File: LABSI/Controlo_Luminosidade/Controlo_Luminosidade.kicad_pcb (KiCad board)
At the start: 2 copper layers, 86 x 71 mm, 38 parts, among them J1 Barrel_Jack_Switch, J2 Barrel_Jack_Switch, J3 Conn_01x05_Pin, J5 Conn_01x04_Pin, J6 AVR-ISP-6, J7 Conn_01x03_Pin, J8 Conn_01x03_Pin, J9 Conn_01x05_Pin, Q1 IRLZ24, U1 ATmega328-P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

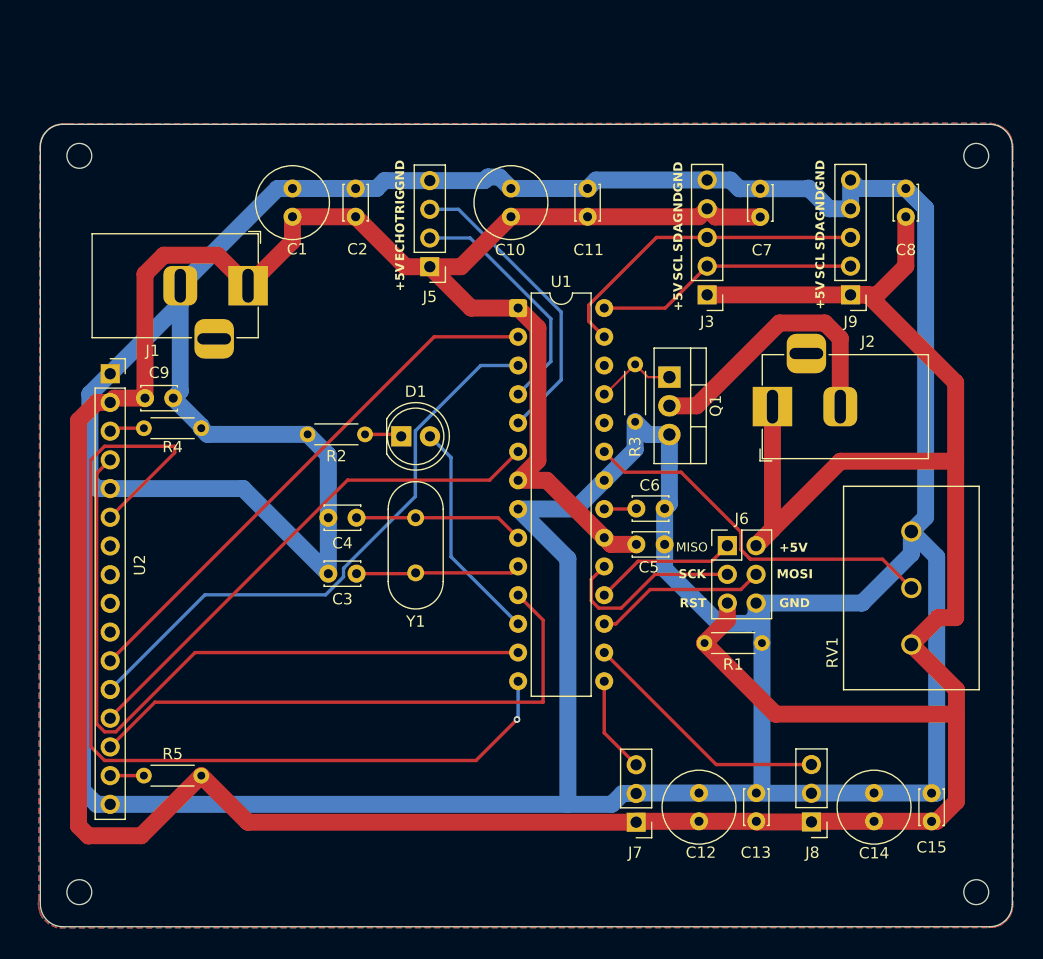
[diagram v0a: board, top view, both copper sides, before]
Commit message: added lcd through i2c, code for timer1(servo)
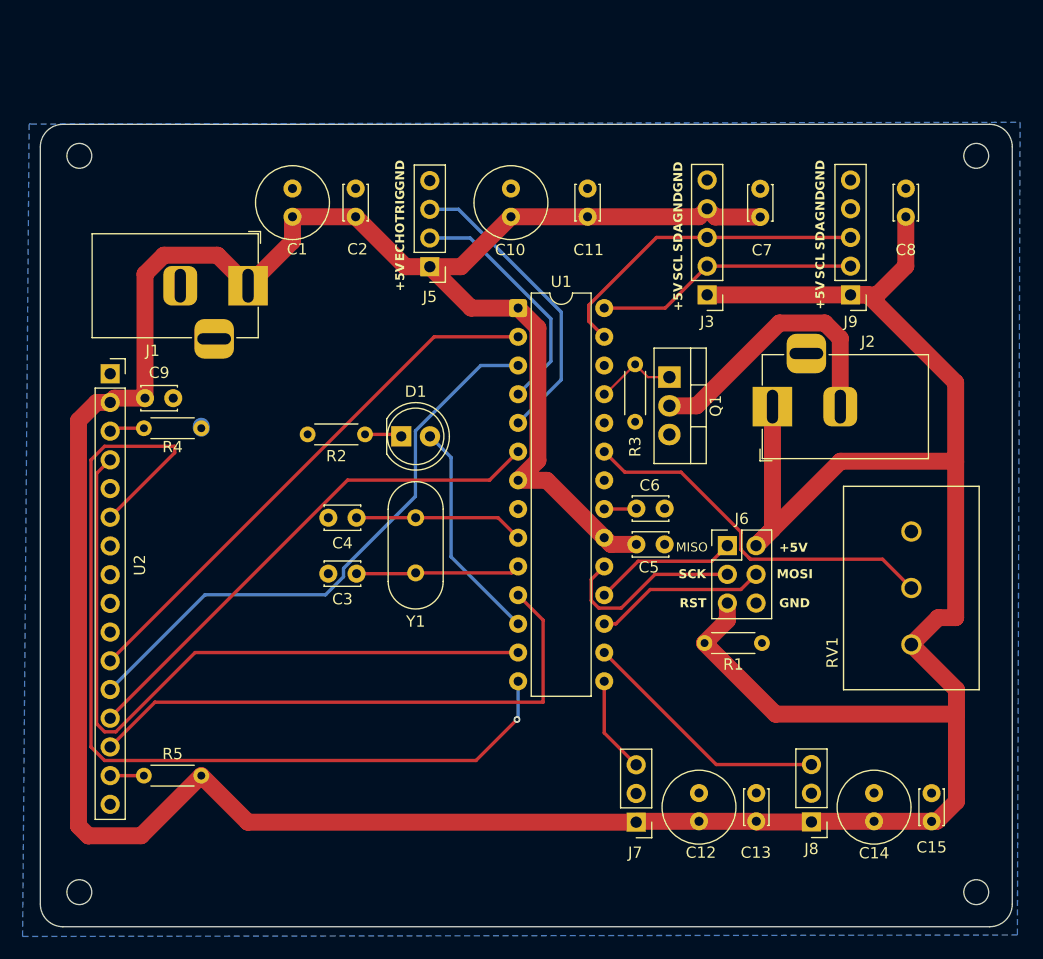
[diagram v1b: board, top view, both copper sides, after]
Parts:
- R2: value 220 -> 330
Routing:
- net GND: track 418.3 -> 0.30 mm
- removed copper zone on F.Cu, net GND

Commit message: botoes touch sem debounce a funcionar, logica motor a funcionar
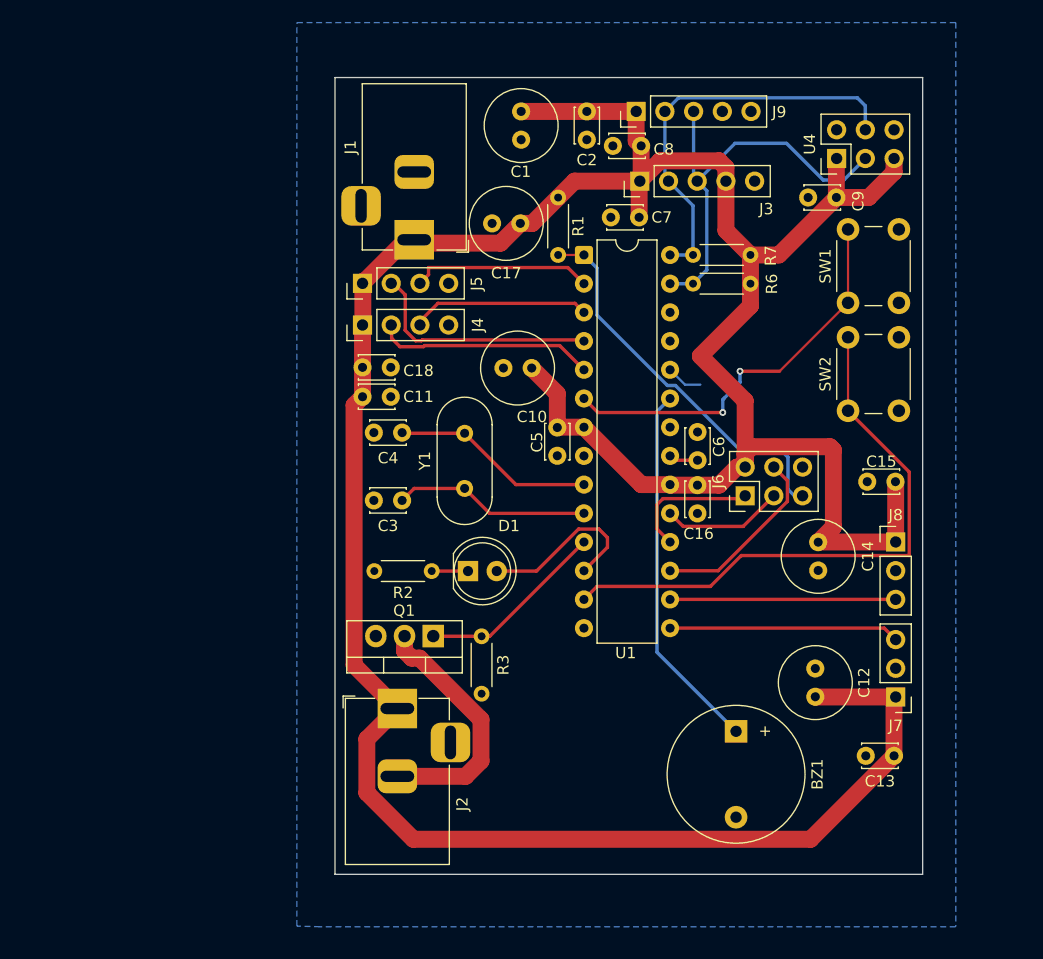
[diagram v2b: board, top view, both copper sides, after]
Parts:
- removed R4: 1k, Resistor_THT:R_Axial_DIN0204_L3.6mm_D1.6mm_P5.08mm_Horizontal
- removed R5: 220, Resistor_THT:R_Axial_DIN0204_L3.6mm_D1.6mm_P5.08mm_Horizontal
- removed REF** (x4): MountingHole_2.2mm_M2, MountingHole:MountingHole_2.2mm_M2
- removed RV1: R_Potentiometer, P160KN-0QC15B500K:P160
- removed U2: LCD1602A, Connector_PinSocket_2.54mm:PinSocket_1x16_P2.54mm_Vertical
- added BZ1: Buzzer, Buzzer_Beeper:Buzzer_12x9.5RM7.6, F.Cu at (160.6, 107.7)
- added C16: 0.1u, Capacitor_THT:C_Disc_D3.0mm_W2.0mm_P2.50mm, F.Cu at (157.1, 85.9)
- added C17: 10u, Capacitor_THT:C_Radial_D6.3mm_H11.0mm_P2.50mm, F.Cu at (141.5, 62.8)
- added C18: 0.1u, Capacitor_THT:C_Disc_D3.0mm_W2.0mm_P2.50mm, F.Cu at (127.5, 75.5)
- added J4: Conn_01x04_Pin, Connector_PinHeader_2.54mm:PinHeader_1x04_P2.54mm_Vertical, F.Cu at (127.5, 71.8)
- added R6: 10k, Resistor_THT:R_Axial_DIN0204_L3.6mm_D1.6mm_P5.08mm_Horizontal, F.Cu at (156.8, 68.1)
- added R7: 10k, Resistor_THT:R_Axial_DIN0204_L3.6mm_D1.6mm_P5.08mm_Horizontal, F.Cu at (156.8, 65.6)
- added SW1: SW_Push, Button_Switch_THT:SW_PUSH_6mm, F.Cu at (170.5, 69.8)
- added SW2: SW_Push, Button_Switch_THT:SW_PUSH_6mm, F.Cu at (170.5, 79.3)
- added U4: I2C_4PIN, Connector_PinHeader_2.54mm:PinHeader_2x03_P2.54mm_Vertical, F.Cu at (169.5, 57.0)
- moved C9 63.7 mm to (169.4, 60.5), turned to 180 degrees
- moved J2 42.6 mm to (130.6, 105.7), turned to 90 degrees
- moved R1 36.7 mm to (144.8, 65.6), turned to 90 degrees
- moved Q1 31.0 mm to (133.8, 99.3), turned to 180 degrees
- moved C15 30.2 mm to (174.7, 85.6), turned to 180 degrees
- moved R3 27.6 mm to (138.0, 99.3)
- moved J8 25.9 mm to (174.7, 91.0), turned to 0 degrees
- moved C11 25.5 mm to (127.5, 78.1), turned to 0 degrees
- moved J7 25.5 mm to (174.7, 104.7)
- moved C14 25.2 mm to (167.8, 91.0), turned to -90 degrees
- moved J9 25.0 mm to (151.7, 52.9), turned to 90 degrees
- moved C8 24.2 mm to (152.2, 55.9), turned to 180 degrees
- moved C2 22.5 mm to (147.4, 52.9), turned to -90 degrees
- moved C1 22.3 mm to (141.5, 52.9), turned to -90 degrees
- moved J1 15.3 mm to (132.1, 64.2), turned to -90 degrees
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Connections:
- J6 pad 5: +5V -> /RST-AVR
- Q1 pad 1: /PC2/GATE -> /PD5/GATE
- R1 pad 1: +5V -> /RST-AVR
- R1 pad 2: GND -> +5V
- R3 pad 1: /PC2/GATE -> /PD5/GATE
- U1 pad 1: +5V -> /RST-AVR
- U1 pad 11: /D7_LCD -> /PD5/GATE
- U1 pad 13: /RS_LCD -> /PD7/SW2
- U1 pad 14: /EN_LCD -> unconnected-(U1-PB0-Pad14)
- U1 pad 2: /D4_LCD -> /TRIG
- U1 pad 23: /PC0/POTENT -> /BUZZER
- U1 pad 24: unconnected-(U1-PC1-Pad24) -> Net-(J10-Pin_2)
- U1 pad 25: /PC2/GATE -> unconnected-(U1-PC2-Pad25)
- U1 pad 3: /D5_LCD -> /TRIG2
- U1 pad 5: /TRIG -> /ECHO2
- U1 pad 6: /D6_LCD -> /PD4/SW1
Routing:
- net +5V: track 379.2 -> 276.7 mm
- net /EN_LCD: track 85.1 -> 0.00 mm, vias 1 -> 0
- net /RS_LCD: track 64.3 -> 0.00 mm
- net /PD7/SW2: track 0.00 -> 51.9 mm
- net /D5_LCD: track 51.8 -> 0.00 mm
- net /D7_LCD: track 50.3 -> 0.00 mm
- net /D4_LCD: track 48.0 -> 0.00 mm
- net /D6_LCD: track 45.9 -> 0.00 mm
- net /PD4/SW1: track 0.00 -> 35.8 mm, vias 0 -> 2
- net /RST-AVR: track 0.00 -> 34.6 mm
- net /PC0/POTENT: track 33.1 -> 0.00 mm
- net /BUZZER: track 0.00 -> 32.8 mm
- net /ECHO2: track 0.00 -> 19.8 mm
- net /PD5/GATE: track 0.00 -> 16.8 mm
- net /TRIG2: track 0.00 -> 15.5 mm
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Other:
- board size 86 x 71 mm -> 52 x 70.5 mm
- board text removed: "+5V"
- board text removed: "ECHO"
- board text removed: "GND"
- board text removed: "MISO"
- board text removed: "MOSI"
- board text removed: "RST"
- board text removed: "SCK"
- board text removed: "SCL"
- board text removed: "SDA"
- board text removed: "TRIG"

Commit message: att
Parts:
- removed SW1, SW2: SW_Push, Button_Switch_THT:SW_PUSH_6mm
- added J10: Touch Button, Connector_PinSocket_2.54mm:PinSocket_1x03_P2.54mm_Vertical, F.Cu at (157.8, 76.2)
- added J11: Touch Button, Connector_PinSocket_2.54mm:PinSocket_1x03_P2.54mm_Vertical, F.Cu at (141.0, 104.8)
- added J12: Touch Button, Connector_PinSocket_2.54mm:PinSocket_1x03_P2.54mm_Vertical, F.Cu at (149.8, 104.8)
- J4, J5: footprint Connector_PinHeader_2.54mm:PinHeader_1x04_P2.54mm_Vertical -> Connector_PinSocket_2.54mm:PinSocket_1x04_P2.54mm_Vertical
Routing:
- net /PD7/SW2: track 51.9 -> 10.1 mm
- net +5V: track 276.7 -> 304.9 mm
- net /PD4/SW1: track 35.8 -> 28.6 mm, vias 2 -> 1
- net Net-(J10-Pin_2): track 3.23 -> 3.86 mm
